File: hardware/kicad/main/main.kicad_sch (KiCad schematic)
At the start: 60 parts, among them J1 USB_C_Receptacle_USB2.0, J10 ENC_LEFT, J11 ENC_RIGHT, J12 UART0, J2 SERVO_L, J3 SERVO_R, J4 Conn_01x02_Pin, J8 Conn_02x10_Odd_Even, Q1 2N7002K, SW1 SW_SPST, SW2 SW_SPST, SW3 SW_SPST, SW4 SW_SPST, U2 AP1117-33, U5 IP5306, U6 ESP32-S3-WROOM-1

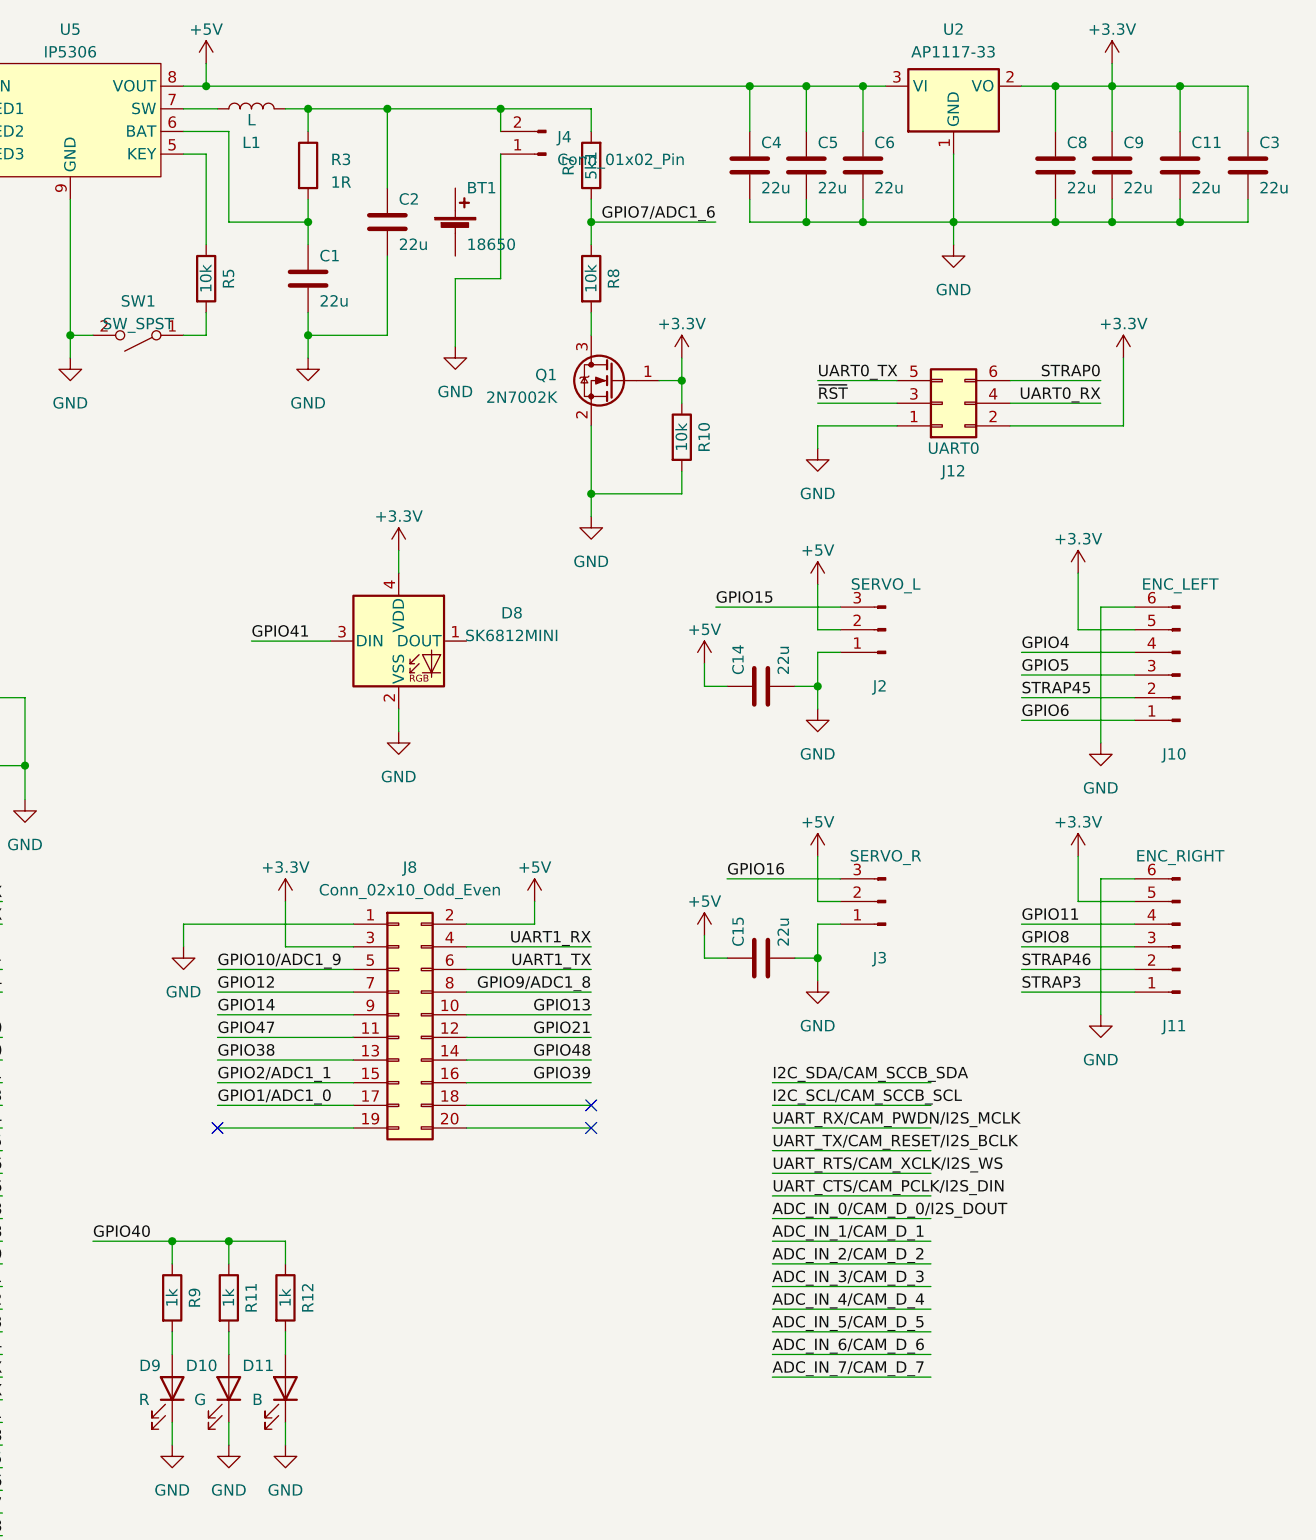
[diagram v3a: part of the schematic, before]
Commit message: changed buttons to basic ones, fixed inductor footprint, added JLCPCB part numbers to each mounted component for assembly
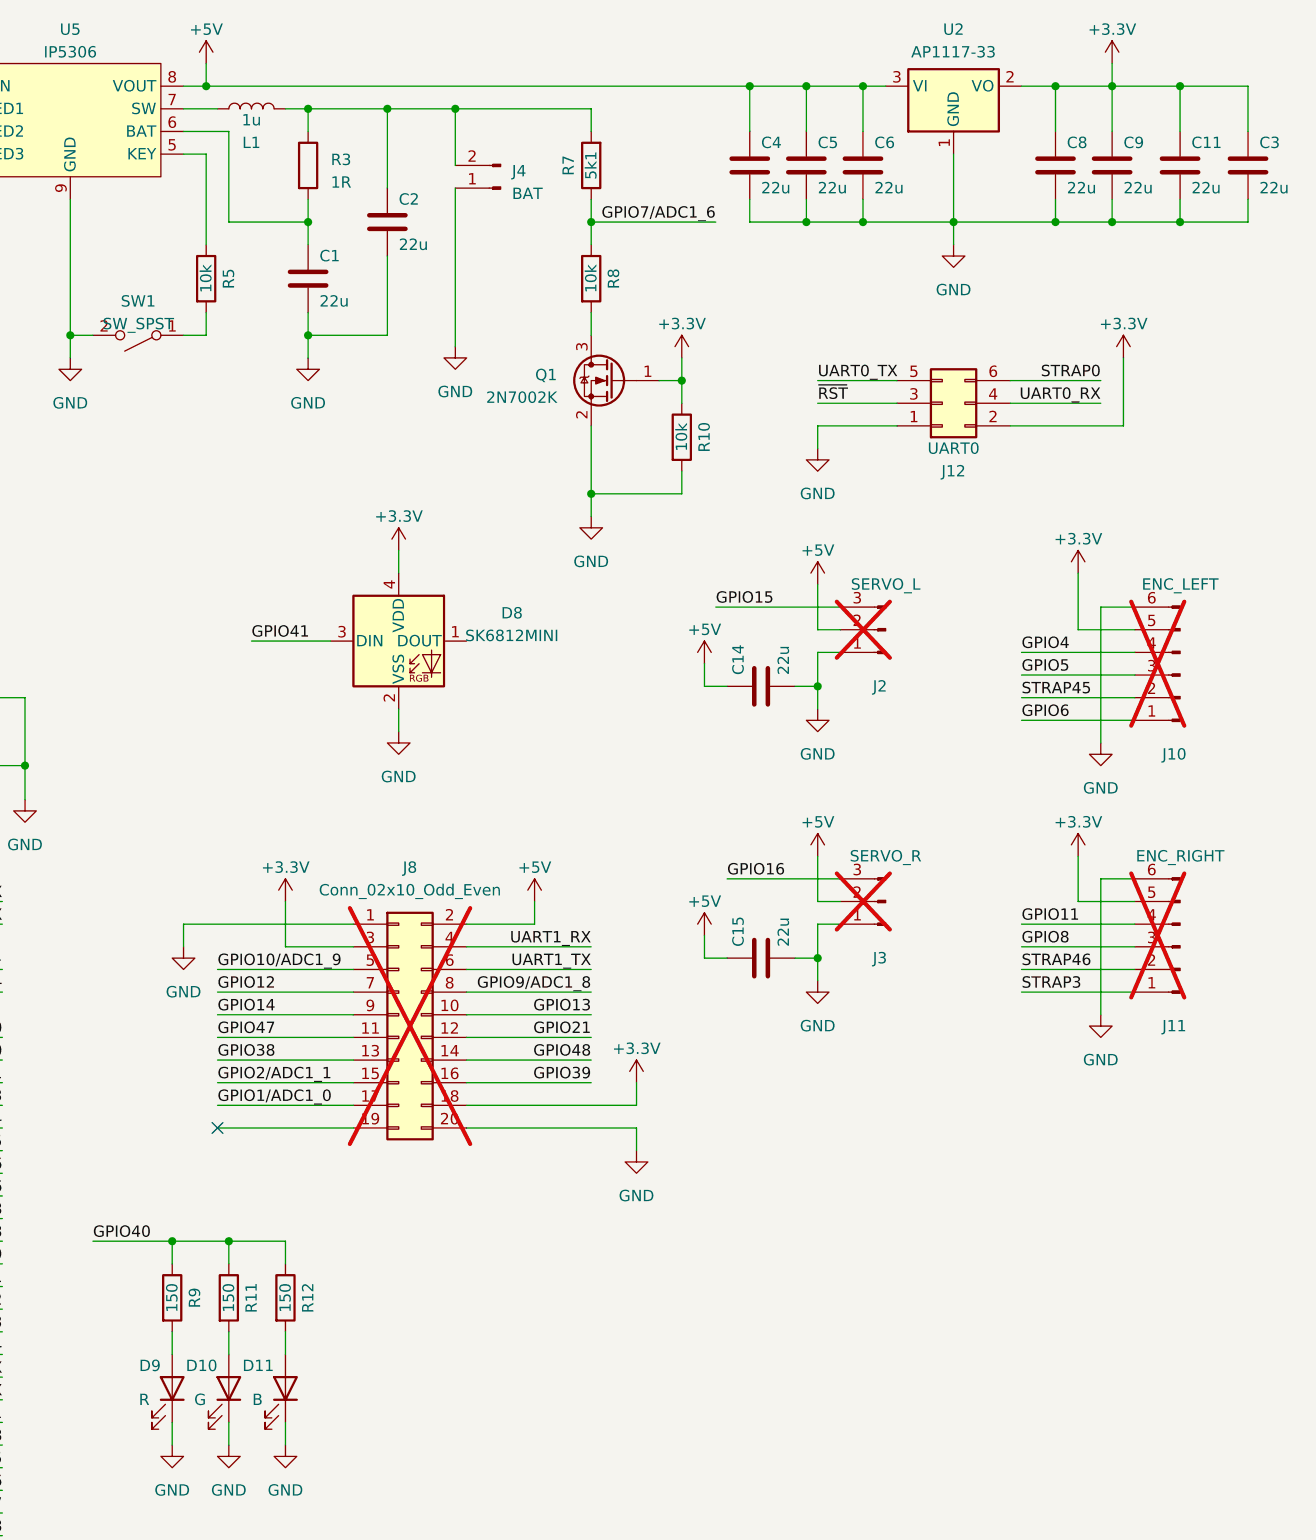
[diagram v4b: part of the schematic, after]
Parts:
- removed BT1: 18650, Battery:BatteryHolder_MPD_BH-18650-PC2, symbol Device:Battery_Cell
- C1, C11, C13, C14, C15, C2, C3, C4, C5, C6, C7, C8, C9: JLCPCB (none) -> C12891
- C10, C12: JLCPCB (none) -> C14663
- D1, D2, D3: JLCPCB (none) -> C5199850; LCSC https://www.lcsc.com/product-detail/span-style-background-c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 -> (none)
- D10: JLCPCB (none) -> C72043
- D11: JLCPCB (none) -> C72041
- D4, D5, D6, D7: JLCPCB (none) -> C2290
- D8: JLCPCB (none) -> C5183448
- D9: JLCPCB (none) -> C2286
- H1, H2, H3, H4: now left out of the parts list
- J1: JLC https://jlcpcb.com/partdetail/ShouHan-TYPE_C_16P_073/C668624 -> (none); JLCPCB (none) -> C668624
- J10, J11, J2, J3: now not fitted; now left out of the parts list
- J4: value Conn_01x02_Pin -> BAT
- J8: JLCPCB (none) -> C124419; now not fitted; now left out of the parts list
- L1: value L -> 1u; footprint Inductor_SMD:L_6.3x6.3_H3 -> Inductor_SMD:L_Changjiang_FNR6020S; JLCPCB (none) -> C436414
- Q1: JLCPCB (none) -> C8545
- R1, R2, R7: JLCPCB (none) -> C23186
- R10, R5, R6, R8: JLCPCB (none) -> C25804
- R11, R12, R9: value 1k -> 150; JLCPCB (none) -> C22808
- R3, R4: JLCPCB (none) -> C22936
- SW1, SW2, SW3, SW4: footprint Button_Switch_SMD:SW_SPST_CK_RS282G05A3 -> Button_Switch_SMD:SW_SPST_SKQG_WithStem; JLCPCB (none) -> C318884
- U2: JLCPCB (none) -> C6186
- U5: JLC https://jlcpcb.com/partdetail/Injoinic-IP5306/C181692 -> (none); JLCPCB (none) -> C181692
- U6: JLCPCB (none) -> C2913202
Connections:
- net +3.3V: now also J8.18 (Pin_18)
- net GND: now also J8.20 (Pin_20)
- no-connect marks 6 -> 4
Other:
- moved on the sheet: J4

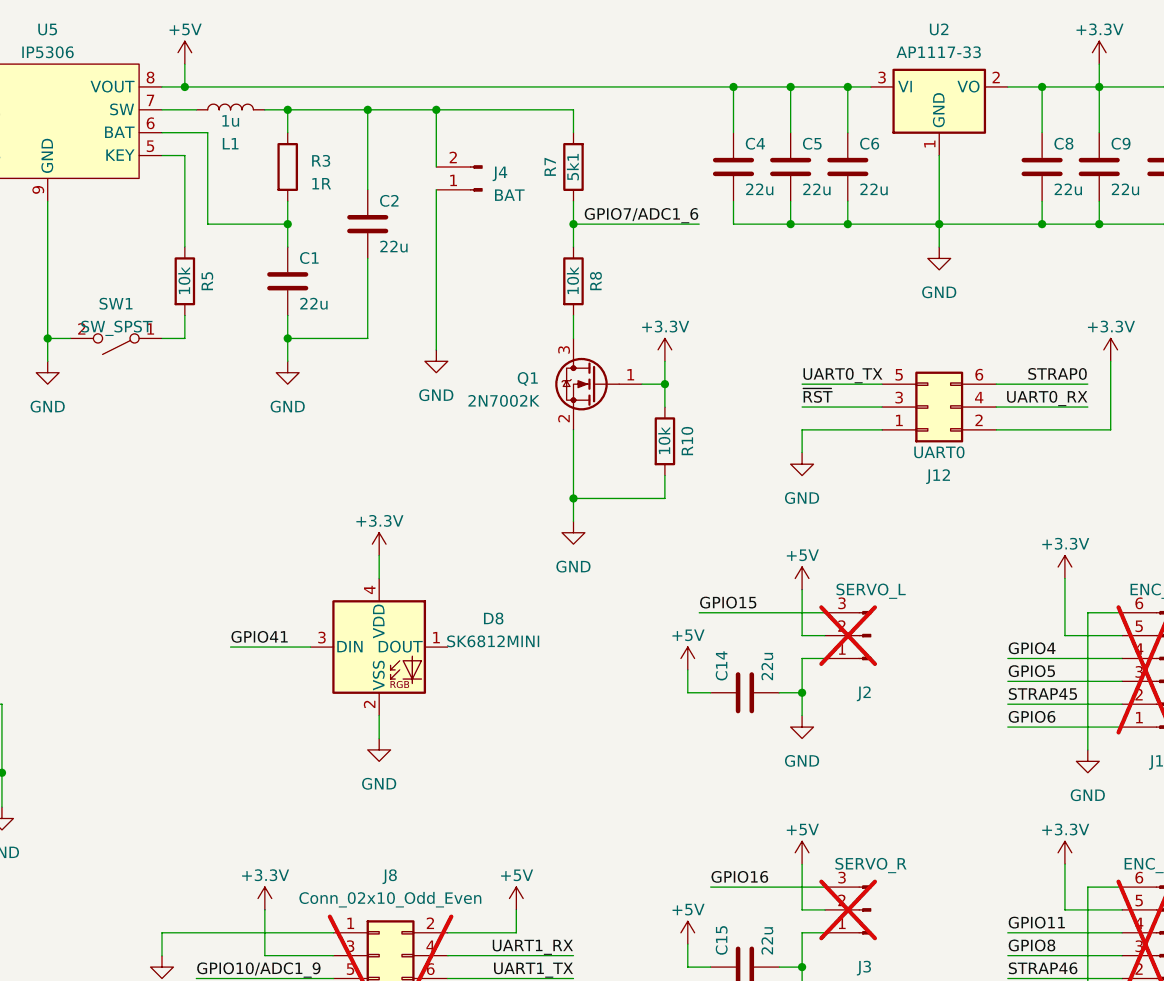
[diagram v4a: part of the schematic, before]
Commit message: removed addressable led as it is not really available, fixed inductor footprint, added production files
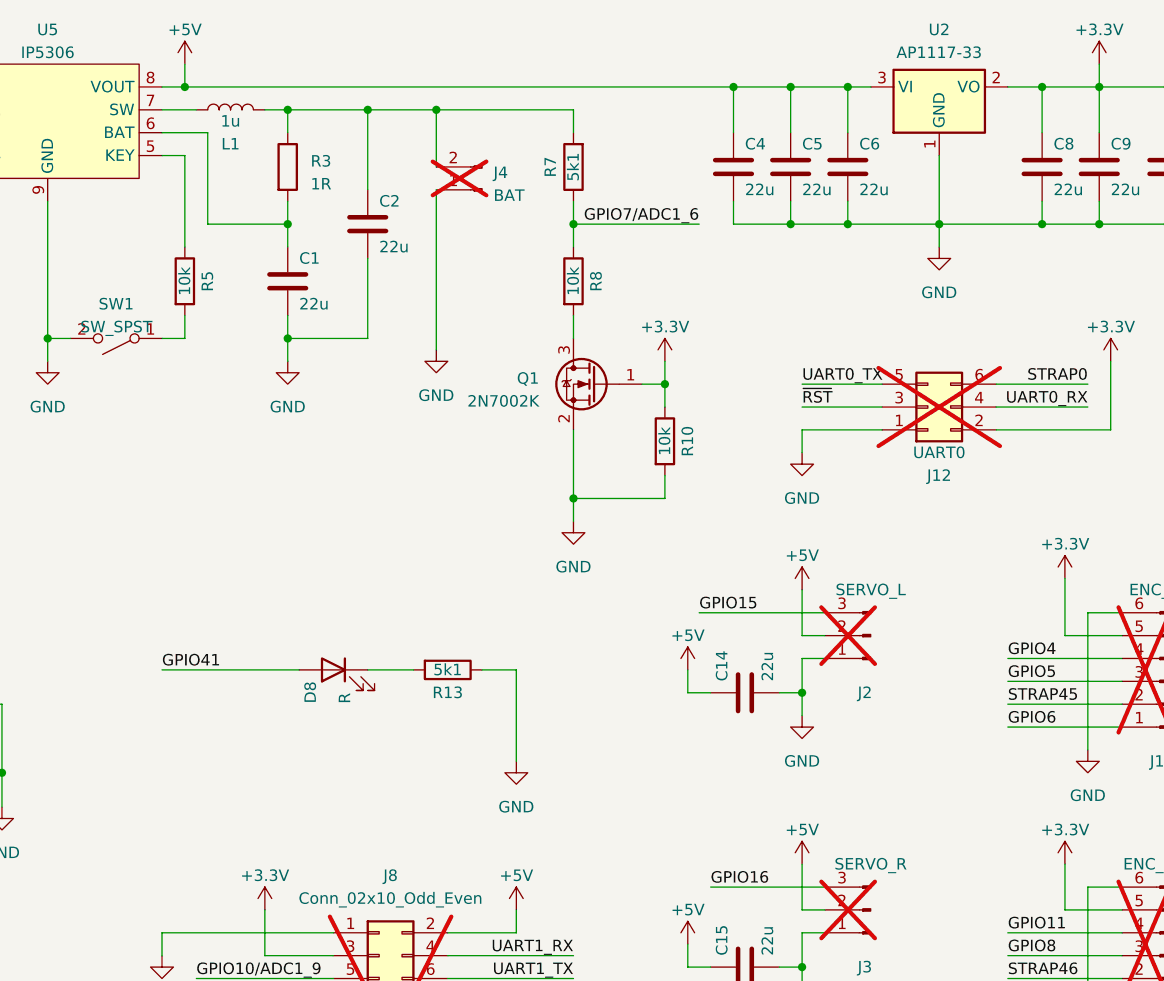
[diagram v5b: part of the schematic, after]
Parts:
- removed D8: SK6812MINI, LED_SMD:LED_SK6812MINI_PLCC4_3.5x3.5mm_P1.75mm, symbol LED:SK6812MINI
- added D8: R, LED_SMD:LED_0603_1608Metric, symbol Device:LED
- added R13: 5k1, Resistor_SMD:R_0603_1608Metric, symbol Device:R
- C1, C11, C13, C14, C15, C2, C3, C4, C5, C6, C7, C8, C9: JLC (none) -> C12891; JLCPCB C12891 -> (none)
- C10, C12: JLC (none) -> C14663; JLCPCB C14663 -> (none)
- D1, D2, D3: JLC (none) -> C383211; JLCPCB C5199850 -> (none)
- D10: JLC (none) -> C72043; JLCPCB C72043 -> (none)
- D11: JLC (none) -> C72041; JLCPCB C72041 -> (none)
- D4, D5, D6, D7: JLC (none) -> C2290; JLCPCB C2290 -> (none)
- D9: JLC (none) -> C2286; JLCPCB C2286 -> (none)
- J1: JLC (none) -> C668624; JLCPCB C668624 -> (none); JLCPCB Position Offset (none) -> 0.0,1.27
- J12, J4: now not fitted; now left out of the parts list
- J8: JLC (none) -> C124419; JLCPCB C124419 -> (none)
- L1: footprint Inductor_SMD:L_Changjiang_FNR6020S -> Inductor_SMD:L_Changjiang_FNR5045S; JLC (none) -> C436396; JLCPCB C436414 -> (none)
- Q1: JLC (none) -> C8545; JLCPCB C8545 -> (none); JLCPCB Rotation Offset (none) -> 180
- R1, R2, R7: JLC (none) -> C23186; JLCPCB C23186 -> (none)
- R10, R5, R6, R8: JLC (none) -> C25804; JLCPCB C25804 -> (none)
- R11, R12, R9: JLC (none) -> C22808; JLCPCB C22808 -> (none)
- R3, R4: JLC (none) -> C22936; JLCPCB C22936 -> (none)
- SW1, SW2, SW3, SW4: JLC (none) -> C318884; JLCPCB C318884 -> (none)
- U2: JLC (none) -> C6186; JLCPCB C6186 -> (none); JLCPCB Rotation Offset (none) -> 180
- U5: JLC (none) -> C181692; JLCPCB C181692 -> (none); JLCPCB Rotation Offset (none) -> -90
- U6: JLC (none) -> C2913202; JLCPCB C2913202 -> (none); JLCPCB Position Offset (none) -> 0.0,-0.65
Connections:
- net GND: now also R13.1
- net GPIO41: now also D8.2 (A)
- new net: D8.1 (K), R13.2

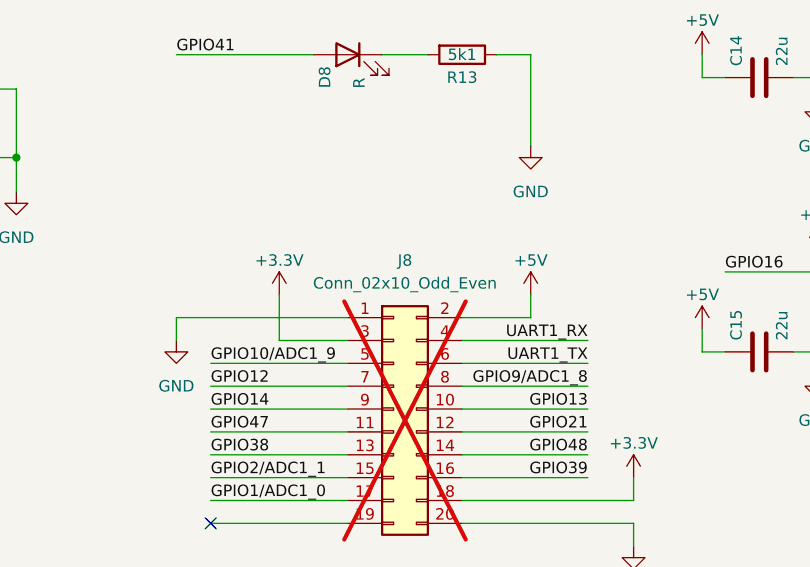
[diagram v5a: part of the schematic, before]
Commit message: added interactive bom, updated blend files with more clearance on 18650 cell
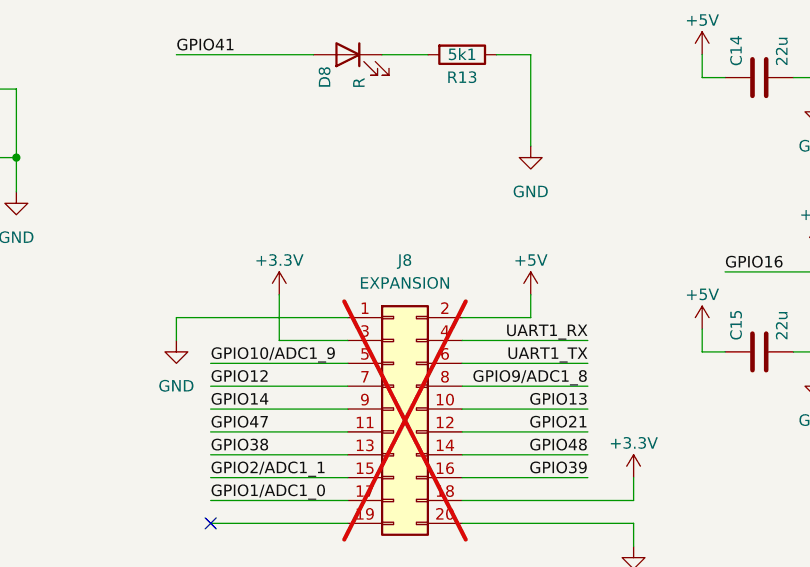
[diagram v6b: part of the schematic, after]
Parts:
- J10, J11, J12, J2, J3, J4: now in the parts list
- J8: value Conn_02x10_Odd_Even -> EXPANSION; now in the parts list
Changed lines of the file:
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@@
   )
   (symbol (lib_id "Connector:Conn_01x06_Pin") (at 269.24 86.36 180) (unit 1)
-    (in_bom no) (on_board yes) (dnp yes)
+    (in_bom yes) (on_board yes) (dnp yes)
     (property "Reference" "J10" (at 268.605 95.25 0)
       (effects (font (size 1.27 1.27)))
@@
   )
   (symbol (lib_id "Connector:Conn_01x06_Pin") (at 269.24 116.84 180) (unit 1)
-    (in_bom no) (on_board yes) (dnp yes)
+    (in_bom yes) (on_board yes) (dnp yes)
     (property "Reference" "J11" (at 268.605 125.73 0)
       (effects (font (size 1.27 1.27)))
@@
   )
   (symbol (lib_id "Connector:Conn_01x02_Pin") (at 193.04 31.75 180) (unit 1)
-    (in_bom no) (on_board yes) (dnp yes) (fields_autoplaced)
+    (in_bom yes) (on_board yes) (dnp yes) (fields_autoplaced)
     (property "Reference" "J4" (at 194.31 29.845 0)
       (effects (font (size 1.27 1.27)) (justify right))
@@
   )
   (symbol (lib_id "Connector_Generic:Conn_02x10_Odd_Even") (at 181.61 124.46 0) (unit 1)
-    (in_bom no) (on_board yes) (dnp yes)
+    (in_bom yes) (on_board yes) (dnp yes)
     (property "Reference" "J8" (at 182.88 107.95 0)
       (effects (font (size 1.27 1.27)))
     )
-    (property "Value" "Conn_02x10_Odd_Even" (at 182.88 110.49 0)
+    (property "Value" "EXPANSION" (at 182.88 110.49 0)
       (effects (font (size 1.27 1.27)))
     )
@@
   )
   (symbol (lib_id "Connector_Generic:Conn_02x03_Odd_Even") (at 242.57 55.88 0) (mirror x) (unit 1)
-    (in_bom no) (on_board yes) (dnp yes)
+    (in_bom yes) (on_board yes) (dnp yes)
     (property "Reference" "J12" (at 243.84 63.5 0)
       (effects (font (size 1.27 1.27)))
@@
   )
   (symbol (lib_id "Connector:Conn_01x03_Pin") (at 236.22 111.76 180) (unit 1)
-    (in_bom no) (on_board yes) (dnp yes)
+    (in_bom yes) (on_board yes) (dnp yes)
     (property "Reference" "J3" (at 235.585 118.11 0)
       (effects (font (size 1.27 1.27)))
@@
   )
   (symbol (lib_id "Connector:Conn_01x03_Pin") (at 236.22 81.28 180) (unit 1)
-    (in_bom no) (on_board yes) (dnp yes)
+    (in_bom yes) (on_board yes) (dnp yes)
     (property "Reference" "J2" (at 235.585 87.63 0)
       (effects (font (size 1.27 1.27)))
